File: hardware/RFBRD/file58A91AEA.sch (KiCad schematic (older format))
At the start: 0 parts

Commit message: Added bits of the RF Board, dumped to PCB.
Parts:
- added C25: C, Capacitors_SMD:C_0805, symbol C
- added C26, C27: 10nF, Capacitors_SMD:C_0805, symbol C
- added C28, C29: 3.193pF, Capacitors_SMD:C_0805, symbol C
- added L16: 10uH, Resistors_SMD:R_0805, symbol INDUCTOR
- added L17: 18nH, Resistors_SMD:R_0805, symbol INDUCTOR
- added L18: 16uH, Choke_SMD:Choke_SMD_12x12mm_h4.5mm, symbol INDUCTOR
- added Q1: Q_NPN_BCE, TO_SOT_Packages_SMD:SOT-23, symbol Q_NPN_BCE
- added R4: 309, Resistors_SMD:R_0603, symbol R
- added R5: 60.4, Resistors_SMD:R_0603, symbol R
- added R6, R7, R8: 10, Resistors_SMD:R_0603, symbol R
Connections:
- new net: C25.1, L16.2, L17.1, R4.1
- new net: C26.1, Q1.1 (B), R4.2, R5.1
- new net: C27.2, L17.2, Q1.2 (C)
- new net: Q1.3 (E), R6.1, R7.1, R8.1
- new net: C27.1, C28.1, L18.1
- new net 5V: L16.1
- new net GND: C25.2, C28.2, C29.2, R5.2, R6.2, R7.2, R8.2
- new net PREAMP_TX: C29.1, L18.2
- new net RF_PREAMP: C26.2

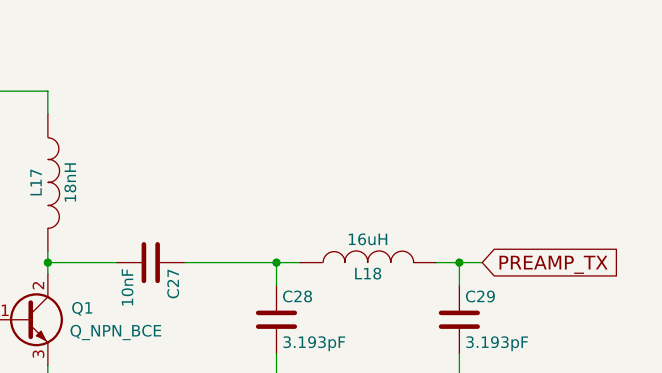
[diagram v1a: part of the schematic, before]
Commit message: Added some Amplification Chain work.
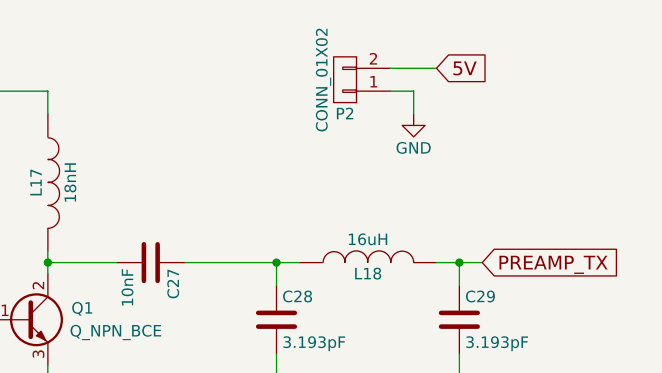
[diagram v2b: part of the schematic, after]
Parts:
- added P2: CONN_01X02, Pin_Headers:Pin_Header_Straight_1x02, symbol CONN_01X02
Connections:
- net 5V: now also P2.2 (P2)
- net GND: now also P2.1 (P1)
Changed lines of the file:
@@
 Text GLabel 4800 1700 2    60   Input ~ 0
 PREAMP_TX
+$Comp
+L CONN_01X02 P2
+U 1 1 58C4C605
+P 4200 900
+F 0 "P2" H 4200 1050 50  0000 C CNN
+F 1 "CONN_01X02" V 4300 900 50  0000 C CNN
+F 2 "Pin_Headers:Pin_Header_Straight_1x02" H 4200 900 50  0001 C CNN
+F 3 "" H 4200 900 50  0000 C CNN
+	1    4200 900
+	-1   0    0    1
+$EndComp
+Wire Wire Line
+	4400 850  4600 850
+Wire Wire Line
+	4400 950  4500 950
+Wire Wire Line
+	4500 950  4500 1050
+$Comp
+L GND #PWR029
+U 1 1 58C4C725
+P 4500 1050
+F 0 "#PWR029" H 4500 800 50  0001 C CNN
+F 1 "GND" H 4500 900 50  0000 C CNN
+F 2 "" H 4500 1050 50  0000 C CNN
+F 3 "" H 4500 1050 50  0000 C CNN
+	1    4500 1050
+	1    0    0    -1
+$EndComp
+Text GLabel 4600 850  2    60   Input ~ 0
+5V
 $EndSCHEMATC
